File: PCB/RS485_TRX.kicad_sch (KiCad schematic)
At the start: 2 parts, among them J1 Conn_01x04, U2 SP3485EN

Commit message: Updated PCB
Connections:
- net GND: now also J1.4 (Pin_4)
- net VIN: now also J1.1 (Pin_1)
- net at U2.6 (A): now also J1.2 (Pin_2)
- net at U2.7 (B): now also J1.3 (Pin_3)
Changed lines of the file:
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@@
 	(generator_version "8.0")
 	(paper "A4")
+	(junction
+		(at 156.21 81.28)
+		(diameter 0)
+		(color 0 0 0 0)
+	)
 	(wire
 		(pts
@@
 	(wire
 		(pts
+			(xy 180.34 97.79) (xy 179.07 97.79)
+		)
+		(stroke
+			(width 0)
+			(type default)
+		)
+	)
+	(wire
+		(pts
+			(xy 166.37 99.06) (xy 172.72 99.06)
+		)
+		(stroke
+			(width 0)
+			(type default)
+		)
+	)
+	(wire
+		(pts
 			(xy 125.73 101.6) (xy 146.05 101.6)
 		)
@@
 	(wire
 		(pts
+			(xy 180.34 105.41) (xy 176.53 105.41)
+		)
+		(stroke
+			(width 0)
+			(type default)
+		)
+	)
+	(wire
+		(pts
+			(xy 179.07 81.28) (xy 156.21 81.28)
+		)
+		(stroke
+			(width 0)
+			(type default)
+		)
+	)
+	(wire
+		(pts
 			(xy 125.73 106.68) (xy 146.05 106.68)
 		)
@@
 	(wire
 		(pts
+			(xy 172.72 99.06) (xy 172.72 100.33)
+		)
+		(stroke
+			(width 0)
+			(type default)
+		)
+	)
+	(wire
+		(pts
 			(xy 156.21 121.92) (xy 156.21 132.08)
+		)
+		(stroke
+			(width 0)
+			(type default)
+		)
+	)
+	(wire
+		(pts
+			(xy 172.72 104.14) (xy 166.37 104.14)
+		)
+		(stroke
+			(width 0)
+			(type default)
+		)
+	)
+	(wire
+		(pts
+			(xy 179.07 97.79) (xy 179.07 81.28)
+		)
+		(stroke
+			(width 0)
+			(type default)
+		)
+	)
+	(wire
+		(pts
+			(xy 180.34 102.87) (xy 172.72 102.87)
+		)
+		(stroke
+			(width 0)
+			(type default)
+		)
+	)
+	(wire
+		(pts
+			(xy 176.53 105.41) (xy 176.53 109.22)
+		)
+		(stroke
+			(width 0)
+			(type default)
+		)
+	)
+	(wire
+		(pts
+			(xy 172.72 100.33) (xy 180.34 100.33)
+		)
+		(stroke
+			(width 0)
+			(type default)
+		)
+	)
+	(wire
+		(pts
+			(xy 172.72 102.87) (xy 172.72 104.14)
 		)
 		(stroke
@@
 					(unit 1)
 				)
+			)
+		)
+	)
+	(symbol
+		(lib_id "power:GND")
+		(at 176.53 109.22 0)
+		(unit 1)
+		(exclude_from_sim no)
+		(in_bom yes)
+		(on_board yes)
+		(dnp no)
+		(fields_autoplaced yes)
+		(property "Reference" "#PWR022"
+			(at 176.53 115.57 0)
+			(effects
+				(font
+					(size 1.27 1.27)
+				)
+				(hide yes)
+			)
+		)
+		(property "Value" "GND"
+			(at 176.53 114.3 0)
+			(effects
+				(font
+					(size 1.27 1.27)
+				)
+			)
+		)
+		(property "Footprint" ""
+			(at 176.53 109.22 0)
+			(effects
+				(font
+					(size 1.27 1.27)
+				)
+				(hide yes)
+			)
+		)
+		(property "Datasheet" ""
+			(at 176.53 109.22 0)
+			(effects
+				(font
+					(size 1.27 1.27)
+				)
+				(hide yes)
+			)
+		)
+		(property "Description" "Power symbol creates a global label with name \"GND\" , ground"
+			(at 176.53 109.22 0)
+			(effects
+				(font
+					(size 1.27 1.27)
+				)
+				(hide yes)
+			)
+		)
+		(pin "1"
+		)
+		(instances
+			(project "IMU_V100"
+				(path "/b6a8d14b-6e32-4628-bf0c-2046877d1cfa/39f78241-e6ef-41bc-bd06-8782906087b7"
+					(reference "#PWR022")
+					(unit 1)
+				)

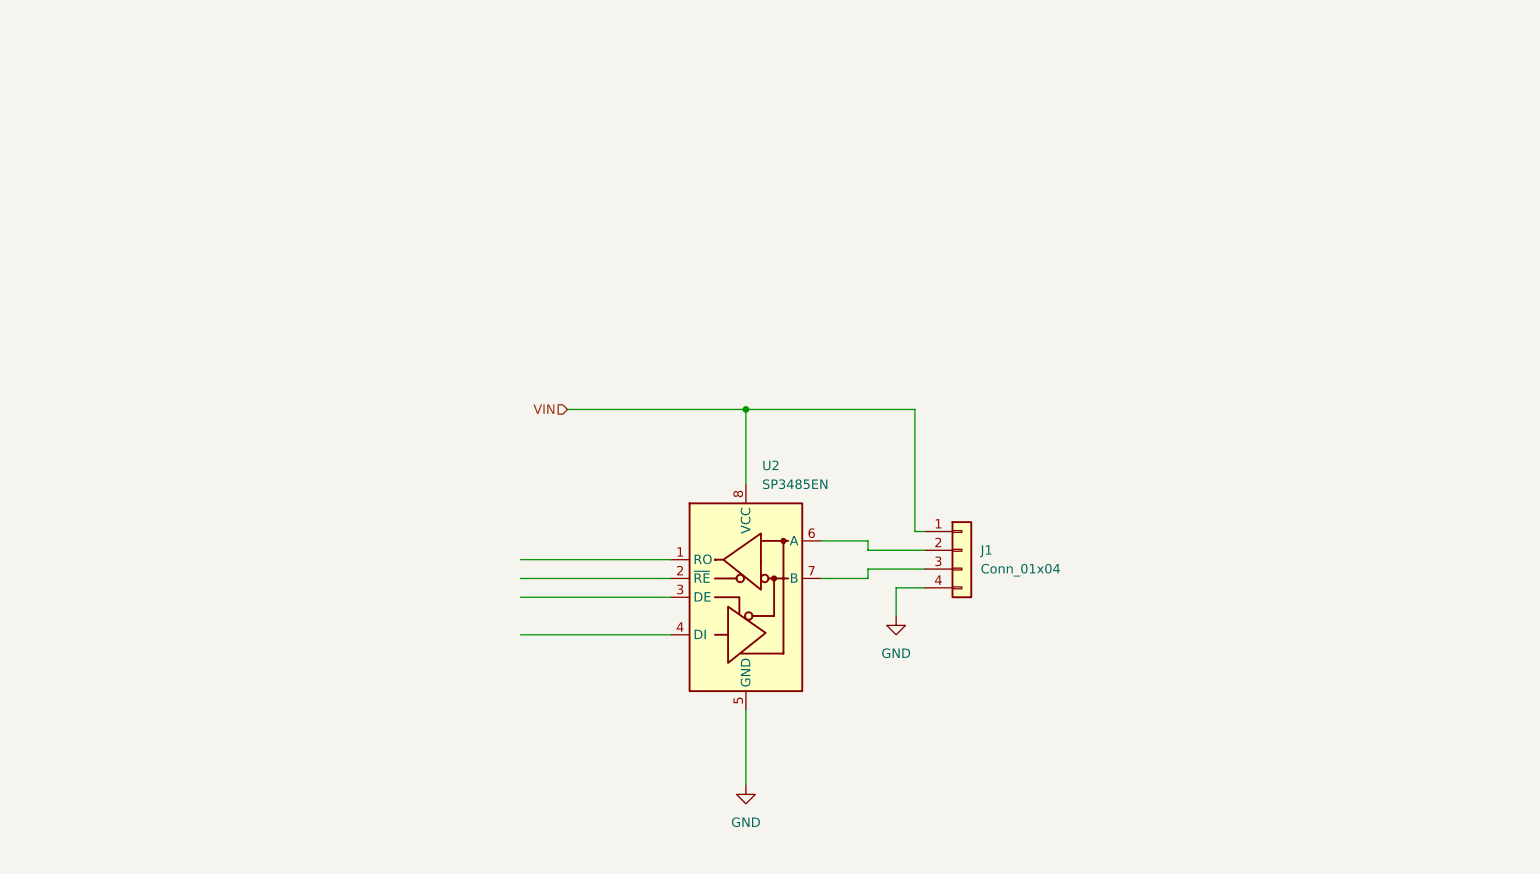
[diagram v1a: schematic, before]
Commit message: Updated PCB. Added Debug section and rectifed RS485
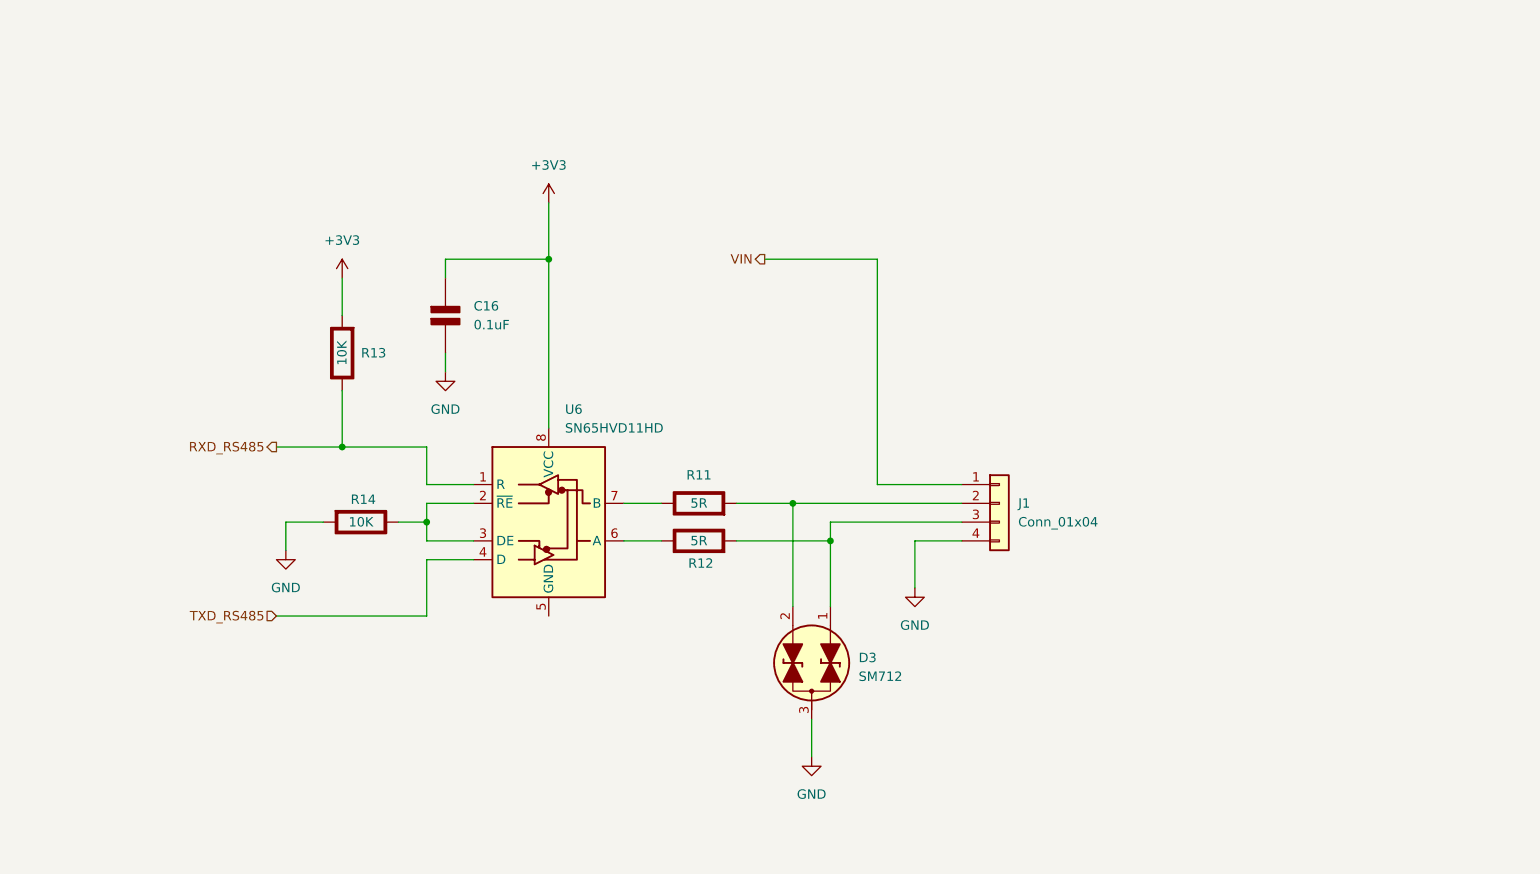
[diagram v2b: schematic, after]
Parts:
- removed U2: SP3485EN, Package_SO:SOIC-8_3.9x4.9mm_P1.27mm, symbol Interface_UART:SP3485EN
- added C16: 0.1uF, symbol PCM_Elektuur:C
- added D3: SM712, PCM_Package_TO_SOT_SMD_AKL:SOT-23, symbol PCM_Diode_TVS_AKL:SM712
- added R11, R12: 5R, symbol PCM_Elektuur:R
- added R13, R14: 10K, symbol PCM_Elektuur:R
- added U6: SN65HVD11HD, Package_SO:SOIC-8_3.9x4.9mm_P1.27mm, symbol Interface_UART:SN65HVD11HD
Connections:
- net GND: now also C16.2 (-), D3.3 (Com), R14.2 (-)
- net at J1.2 (Pin_2): now also D3.2 (A2), R11.2 (-)
- net at J1.3 (Pin_3): now also D3.1 (A1), R12.2 (-)
- new net: R11.1 (+), U6.7 (B)
- new net: R14.1 (+), U6.2 (~{RE}), U6.3 (DE)
- new net: R12.1 (+), U6.6 (A)
- new net +3V3: C16.1 (+), R13.2 (-), U6.8 (VCC)
- new net RXD_RS485: R13.1 (+), U6.1 (R)
- new net TXD_RS485: U6.4 (D)

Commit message: Updated PCB.
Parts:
- renumbered C16 to C18, D3 to D7, J1 to J4, R13 to R14, R14 to R15, R11 to R16, R12 to R17, U6 to U5
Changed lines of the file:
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@@
+		(dnp no)
+		(fields_autoplaced yes)
+		(property "Reference" "#PWR026"
+			(at 93.98 106.68 0)
+			(effects
+				(font
+					(size 1.27 1.27)
+				)
+				(hide yes)
+			)
+		)
+		(property "Value" "GND"
+			(at 93.98 105.41 0)
+			(effects
+				(font
+					(size 1.27 1.27)
+				)
+			)
+		)
+		(property "Footprint" ""
+			(at 93.98 100.33 0)
+			(effects
+				(font
+					(size 1.27 1.27)
+				)
+				(hide yes)
+			)
+		)
+		(property "Datasheet" ""
+			(at 93.98 100.33 0)
+			(effects
+				(font
+					(size 1.27 1.27)
+				)
+				(hide yes)
+			)
+		)
+		(property "Description" "Power symbol creates a global label with name \"GND\" , ground"
+			(at 93.98 100.33 0)
+			(effects
+				(font
+					(size 1.27 1.27)
+				)
+				(hide yes)
+			)
+		)
+		(pin "1"
+		)
+		(instances
+			(project "IMU_V100"
+				(path "/b6a8d14b-6e32-4628-bf0c-2046877d1cfa/205555cc-3b86-4915-975e-3a7e3eed6661/84e3f5e1-ab68-44f3-8700-c3af58140fdb"
+					(reference "#PWR026")
+					(unit 1)
+				)
+			)
+		)
+	)
+	(symbol
+		(lib_id "power:GND")
+		(at 115.57 76.2 0)
+		(unit 1)
+		(exclude_from_sim no)
+		(in_bom yes)
+		(on_board yes)
 		(dnp no)
 		(fields_autoplaced yes)
 		(property "Reference" "#PWR028"
-			(at 93.98 106.68 0)
-			(effects
-				(font
-					(size 1.27 1.27)
-				)
-				(hide yes)
-			)
-		)
-		(property "Value" "GND"
-			(at 93.98 105.41 0)
-			(effects
-				(font
-					(size 1.27 1.27)
-				)
-			)
-		)
-		(property "Footprint" ""
-			(at 93.98 100.33 0)
-			(effects
-				(font
-					(size 1.27 1.27)
-				)
-				(hide yes)
-			)
-		)
-		(property "Datasheet" ""
-			(at 93.98 100.33 0)
-			(effects
-				(font
-					(size 1.27 1.27)
-				)
-				(hide yes)
-			)
-		)
-		(property "Description" "Power symbol creates a global label with name \"GND\" , ground"
-			(at 93.98 100.33 0)
-			(effects
-				(font
-					(size 1.27 1.27)
-				)
-				(hide yes)
-			)
-		)
-		(pin "1"
-		)
-		(instances
-			(project "IMU_V100"
-				(path "/b6a8d14b-6e32-4628-bf0c-2046877d1cfa/39f78241-e6ef-41bc-bd06-8782906087b7"
-					(reference "#PWR028")
-					(unit 1)
-				)
-			)
-		)
-	)
-	(symbol
-		(lib_id "power:GND")
-		(at 115.57 76.2 0)
-		(unit 1)
-		(exclude_from_sim no)
-		(in_bom yes)
-		(on_board yes)
-		(dnp no)
-		(fields_autoplaced yes)
-		(property "Reference" "#PWR024"
 			(at 115.57 82.55 0)
 			(effects
@@
 		)
 		(instances
-			(project ""
-				(path "/b6a8d14b-6e32-4628-bf0c-2046877d1cfa/39f78241-e6ef-41bc-bd06-8782906087b7"
-					(reference "#PWR024")
+			(project "IMU_V100"
+				(path "/b6a8d14b-6e32-4628-bf0c-2046877d1cfa/205555cc-3b86-4915-975e-3a7e3eed6661/84e3f5e1-ab68-44f3-8700-c3af58140fdb"
+					(reference "#PWR028")
 					(unit 1)
 				)
@@
 		(on_board yes)
 		(dnp no)
-		(property "Reference" "R13"
+		(property "Reference" "R14"
 			(at 104.14 73.6599 0)
 			(effects
@@
 		(instances
 			(project "IMU_V100"
-				(path "/b6a8d14b-6e32-4628-bf0c-2046877d1cfa/39f78241-e6ef-41bc-bd06-8782906087b7"
-					(reference "R13")
+				(path "/b6a8d14b-6e32-4628-bf0c-2046877d1cfa/205555cc-3b86-4915-975e-3a7e3eed6661/84e3f5e1-ab68-44f3-8700-c3af58140fdb"
+					(reference "R14")
 					(unit 1)
 				)
@@
 		(dnp no)
 		(fields_autoplaced yes)
-		(property "Reference" "R11"
+		(property "Reference" "R16"
 			(at 149.86 90.17 90)
 			(effects
@@
 		)
 		(instances
-			(project ""
-				(path "/b6a8d14b-6e32-4628-bf0c-2046877d1cfa/39f78241-e6ef-41bc-bd06-8782906087b7"
-					(reference "R11")
+			(project "IMU_V100"
+				(path "/b6a8d14b-6e32-4628-bf0c-2046877d1cfa/205555cc-3b86-4915-975e-3a7e3eed6661/84e3f5e1-ab68-44f3-8700-c3af58140fdb"
+					(reference "R16")
 					(unit 1)
 				)
@@
 		(dnp no)
 		(fields_autoplaced yes)
-		(property "Reference" "J1"
+		(property "Reference" "J4"
 			(at 193.04 93.9799 0)
 			(effects
@@
 		(instances
 			(project "IMU_V100"
-				(path "/b6a8d14b-6e32-4628-bf0c-2046877d1cfa/39f78241-e6ef-41bc-bd06-8782906087b7"
-					(reference "J1")
+				(path "/b6a8d14b-6e32-4628-bf0c-2046877d1cfa/205555cc-3b86-4915-975e-3a7e3eed6661/84e3f5e1-ab68-44f3-8700-c3af58140fdb"
+					(reference "J4")
 					(unit 1)
 				)
@@
 		(dnp no)
 		(fields_autoplaced yes)
-		(property "Reference" "#PWR026"
+		(property "Reference" "#PWR031"
 			(at 179.07 111.76 0)
 			(effects
@@
 		(instances
 			(project "IMU_V100"
-				(path "/b6a8d14b-6e32-4628-bf0c-2046877d1cfa/39f78241-e6ef-41bc-bd06-8782906087b7"
-					(reference "#PWR026")
+				(path "/b6a8d14b-6e32-4628-bf0c-2046877d1cfa/205555cc-3b86-4915-975e-3a7e3eed6661/84e3f5e1-ab68-44f3-8700-c3af58140fdb"
+					(reference "#PWR031")
 					(unit 1)
 				)
@@
 		(dnp no)
 		(fields_autoplaced yes)
-		(property "Reference" "C16"
+		(property "Reference" "C18"
 			(at 119.38 67.3099 0)
 			(effects
@@
 		)
 		(instances
-			(project ""
-				(path "/b6a8d14b-6e32-4628-bf0c-2046877d1cfa/39f78241-e6ef-41bc-bd06-8782906087b7"
-					(reference "C16")
+			(project "IMU_V100"
+				(path "/b6a8d14b-6e32-4628-bf0c-2046877d1cfa/205555cc-3b86-4915-975e-3a7e3eed6661/84e3f5e1-ab68-44f3-8700-c3af58140fdb"
+					(reference "C18")
 					(unit 1)
 				)
@@
 		(dnp no)
 		(fields_autoplaced yes)
-		(property "Reference" "#PWR023"
+		(property "Reference" "#PWR030"
 			(at 165.1 134.62 0)
 			(effects
@@
 		(instances
 			(project "IMU_V100"
-				(path "/b6a8d14b-6e32-4628-bf0c-2046877d1cfa/39f78241-e6ef-41bc-bd06-8782906087b7"
-					(reference "#PWR023")
+				(path "/b6a8d14b-6e32-4628-bf0c-2046877d1cfa/205555cc-3b86-4915-975e-3a7e3eed6661/84e3f5e1-ab68-44f3-8700-c3af58140fdb"
+					(reference "#PWR030")
 					(unit 1)
 				)
@@
 		(dnp no)
 		(fields_autoplaced yes)
-		(property "Reference" "U6"
+		(property "Reference" "U5"
 			(at 131.7341 81.28 0)
 			(effects
@@
 		)
 		(instances
-			(project ""
-				(path "/b6a8d14b-6e32-4628-bf0c-2046877d1cfa/39f78241-e6ef-41bc-bd06-8782906087b7"
-					(reference "U6")
+			(project "IMU_V100"
+				(path "/b6a8d14b-6e32-4628-bf0c-2046877d1cfa/205555cc-3b86-4915-975e-3a7e3eed6661/84e3f5e1-ab68-44f3-8700-c3af58140fdb"
+					(reference "U5")
 					(unit 1)
 				)
@@
 		(on_board yes)
 		(dnp no)
-		(property "Reference" "R12"
+		(property "Reference" "R17"
 			(at 150.114 102.108 90)
 			(effects
@@
 		(instances
 			(project "IMU_V100"
-				(path "/b6a8d14b-6e32-4628-bf0c-2046877d1cfa/39f78241-e6ef-41bc-bd06-8782906087b7"
-					(reference "R12")
+				(path "/b6a8d14b-6e32-4628-bf0c-2046877d1cfa/205555cc-3b86-4915-975e-3a7e3eed6661/84e3f5e1-ab68-44f3-8700-c3af58140fdb"
+					(reference "R17")
 					(unit 1)
 				)
@@
 		(dnp no)
 		(fields_autoplaced yes)
-		(property "Reference" "D3"
+		(property "Reference" "D7"
 			(at 171.45 114.8714 90)
 			(effects
@@
 		(instances
 			(project "IMU_V100"
-				(path "/b6a8d14b-6e32-4628-bf0c-2046877d1cfa/39f78241-e6ef-41bc-bd06-8782906087b7"
-					(reference "D3")
+				(path "/b6a8d14b-6e32-4628-bf0c-2046877d1cfa/205555cc-3b86-4915-975e-3a7e3eed6661/84e3f5e1-ab68-44f3-8700-c3af58140fdb"
+					(reference "D7")
 					(unit 1)
 				)
@@
 		(instances
 			(project "IMU_V100"
-				(path "/b6a8d14b-6e32-4628-bf0c-2046877d1cfa/39f78241-e6ef-41bc-bd06-8782906087b7"
+				(path "/b6a8d14b-6e32-4628-bf0c-2046877d1cfa/205555cc-3b86-4915-975e-3a7e3eed6661/84e3f5e1-ab68-44f3-8700-c3af58140fdb"
 					(reference "#PWR027")
 					(unit 1)
@@
 		(on_board yes)
 		(dnp no)
-		(property "Reference" "R14"
+		(property "Reference" "R15"
 			(at 106.172 93.472 90)
 			(effects
@@
 		(instances
 			(project "IMU_V100"
-				(path "/b6a8d14b-6e32-4628-bf0c-2046877d1cfa/39f78241-e6ef-41bc-bd06-8782906087b7"
-					(reference "R14")
+				(path "/b6a8d14b-6e32-4628-bf0c-2046877d1cfa/205555cc-3b86-4915-975e-3a7e3eed6661/84e3f5e1-ab68-44f3-8700-c3af58140fdb"
+					(reference "R15")
 					(unit 1)
 				)
@@
 		(dnp no)
 		(fields_autoplaced yes)
-		(property "Reference" "#PWR025"
+		(property "Reference" "#PWR029"
 			(at 129.54 57.15 0)
 			(effects
@@
 		)
 		(instances
-			(project ""
-				(path "/b6a8d14b-6e32-4628-bf0c-2046877d1cfa/39f78241-e6ef-41bc-bd06-8782906087b7"
-					(reference "#PWR025")
-					(unit 1)
-				)
+			(project "IMU_V100"
+				(path "/b6a8d14b-6e32-4628-bf0c-2046877d1cfa/205555cc-3b86-4915-975e-3a7e3eed6661/84e3f5e1-ab68-44f3-8700-c3af58140fdb"
+					(reference "#PWR029")
+					(unit 1)
+				)

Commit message: Updated PCB.
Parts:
- removed J4: Conn_01x04, Connector_JST:JST_XH_S4B-XH-A_1x04_P2.50mm_Horizontal, symbol Connector_Generic:Conn_01x04
- added J4: 1-770969-0, Footprints:17709690, symbol IMU_V100:1-770969-0
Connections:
- net GND: now also J4.4
- net VIN: now also J4.1
- net at D7.2 (A2), R16.2 (-): now also J4.2
- net at D7.1 (A1), R17.2 (-): now also J4.5

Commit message: Updated PCB
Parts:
- removed D7: SM712, PCM_Package_TO_SOT_SMD_AKL:SOT-23, symbol PCM_Diode_TVS_AKL:SM712
- removed R16, R17: 5R, symbol PCM_Elektuur:R
- removed U5: SN65HVD11HD, Package_SO:SOIC-8_3.9x4.9mm_P1.27mm, symbol Interface_UART:SN65HVD11HD
- added D8: SM712, PCM_Package_TO_SOT_SMD_AKL:SOT-23, symbol PCM_Diode_TVS_AKL:SM712
- added F1, F2: Polyfuse, symbol Device:Polyfuse
- added R20, R21: 10R, symbol PCM_Elektuur:R
- added U6: THVD1450DR, Package_SON:VSON-8-1EP_3x3mm_P0.65mm_EP1.6x2.4mm, symbol Interface_UART:THVD1450DR
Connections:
- net +3V3: now also U6.8 (VCC)
- net GND: now also D8.3 (Com)
- net RXD_RS485: now also U6.1 (RO)
- net TXD_RS485: now also U6.4 (DI)
- net at J4.2: now also F1.2
- net RS485_USER1: now reaches J4.3
- net at J4.5: now also F2.2
- net RS485_USER2: now reaches J4.6
- net at R15.1 (+): now also U6.2 (~{RE}), U6.3 (DE)
- new net: R21.1 (+), U6.7 (B)
- new net: D8.1 (A1), F2.1, R21.2 (-)
- new net: D8.2 (A2), F1.1, R20.2 (-)
- new net: R20.1 (+), U6.6 (A)
